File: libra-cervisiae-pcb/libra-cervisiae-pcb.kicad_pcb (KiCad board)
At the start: 2 copper layers, 63.8 x 43.2 mm, 24 parts, among them CN1 CP2102-BREAKOUT, CN2 HX711_BREAKOUT, J1 Wort Temp, J2 Ambient Temp, J3 Load Cells, SW1 Reset, SW2 Flash, U1 ESP32-WROOM-32, U2 VREG

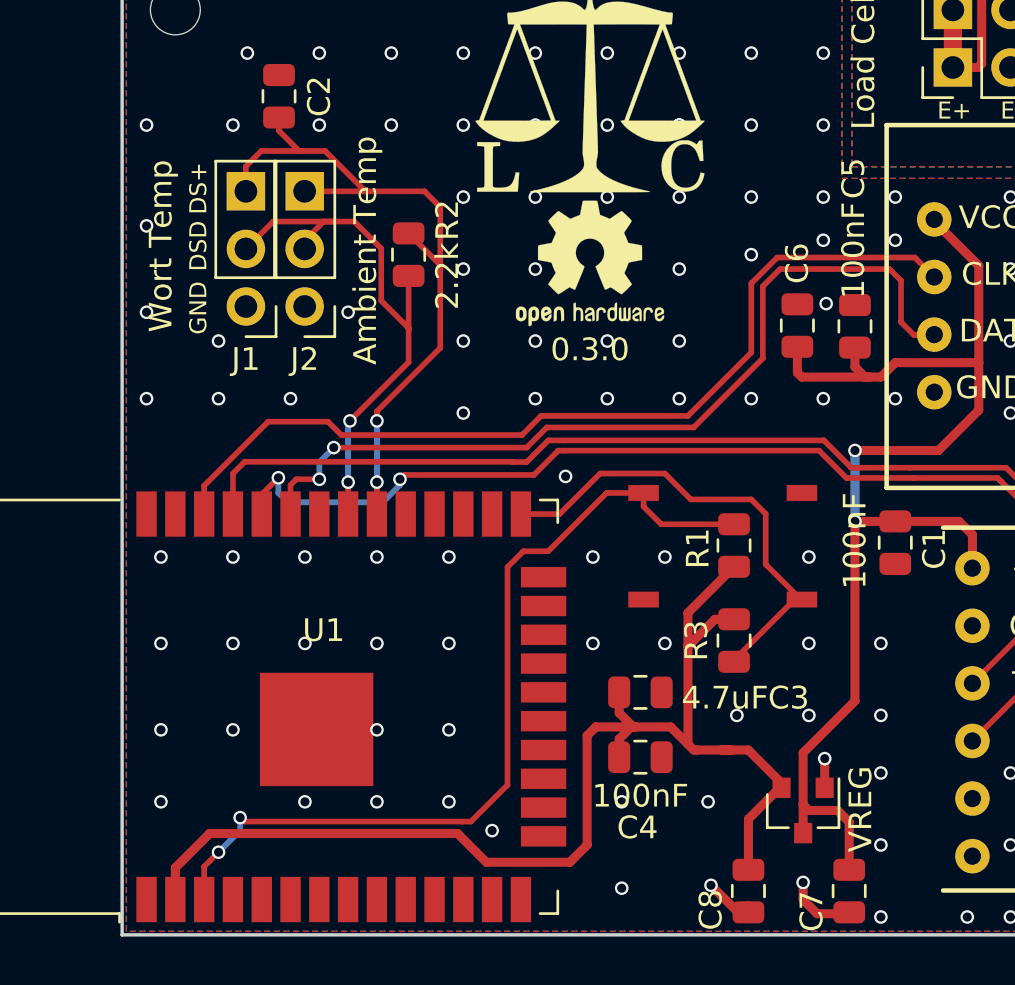
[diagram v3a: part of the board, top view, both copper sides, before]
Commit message: Add a Hotspot button to restart into hotspot mode
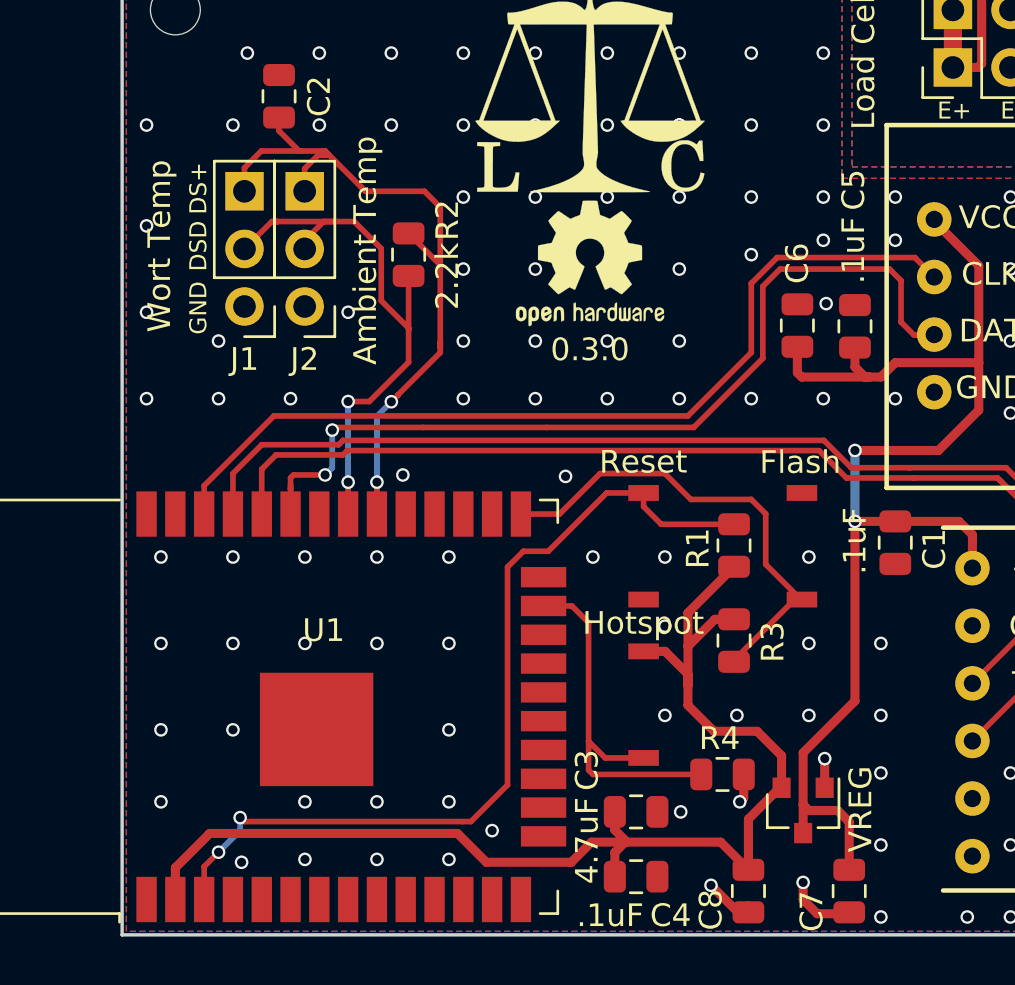
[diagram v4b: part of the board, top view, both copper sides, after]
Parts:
- added R4: 10k, Resistor_SMD:R_0805_2012Metric, F.Cu at (132.7, 101.7)
- added SW3: Hotspot, 4x3_SWITCH:4x3_Switch, F.Cu at (127.6, 95.9)
- C1, C4, C5: value 100nF -> .1uF
- moved C3 5.27 mm to (128.9, 103.3)
- moved C4 5.27 mm to (128.9, 106.2)
- moved J1 0.06 mm to (111.6, 81.0)
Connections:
- U1 pad 23: (no net) -> Net-(R4-Pad2)
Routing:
- net Net-(R4-Pad2): track 0.00 -> 16.4 mm
- net /GND: track 7.01 -> 8.29 mm, vias 164 -> 167
- net /DAT: track 38.1 -> 39.0 mm
- net /DSD: track 24.7 -> 25.5 mm
- net /HostTX: track 46.5 -> 46.6 mm, vias 2 -> 0

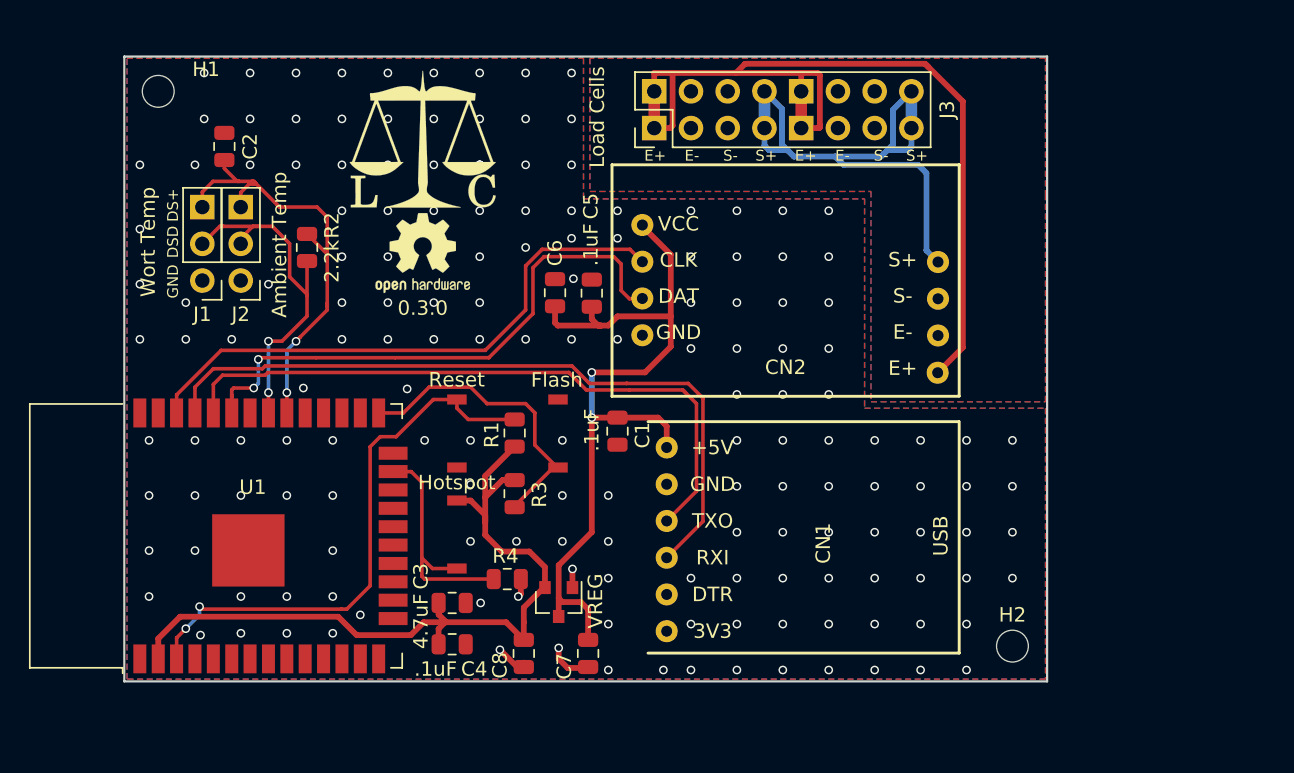
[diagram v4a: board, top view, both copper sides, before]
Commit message: Redo board to DP8049 size
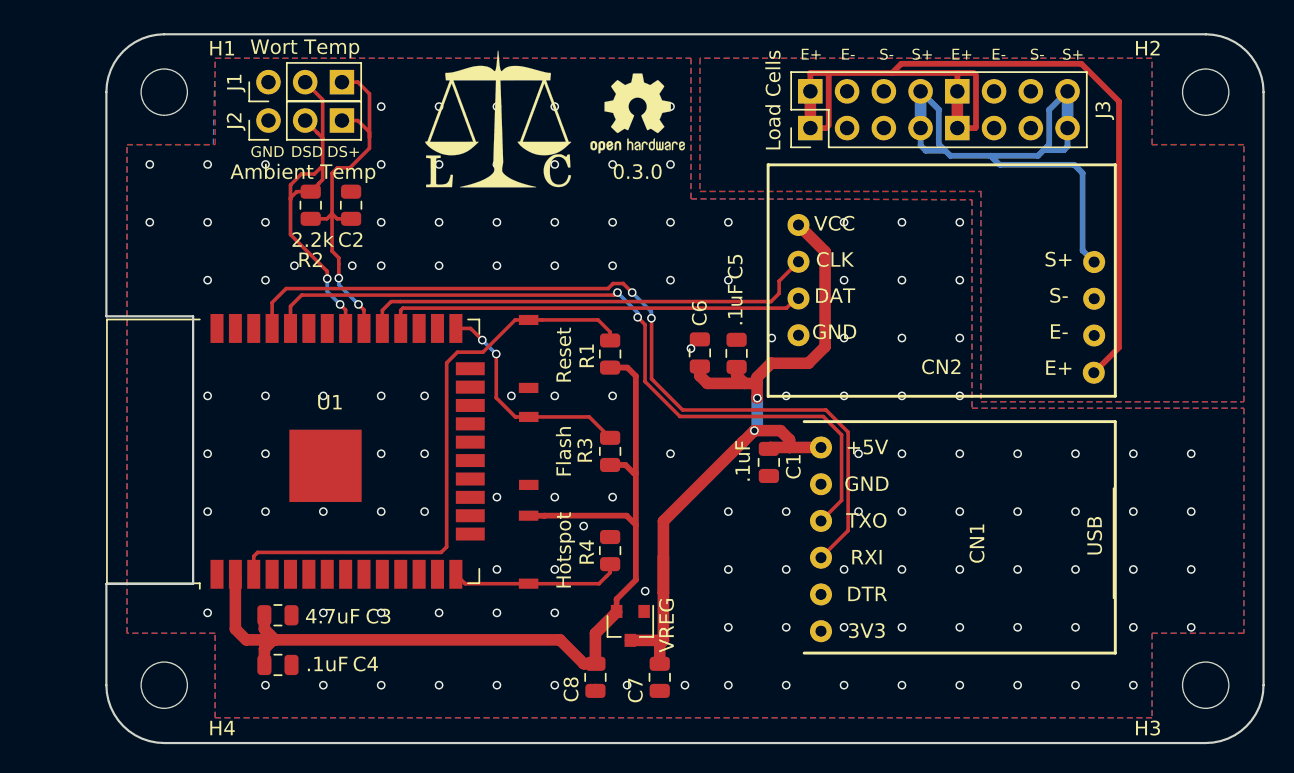
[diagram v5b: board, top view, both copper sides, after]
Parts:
- added H3: MountingHole_3.2mm_M3, MountingHole:MountingHole_3.2mm_M3, F.Cu at (181.0, 109.0)
- added H4: MountingHole_3.2mm_M3, MountingHole:MountingHole_3.2mm_M3, F.Cu at (109.0, 109.0)
- H1, H2: value MountingHole_2.2mm_M2 -> MountingHole_3.2mm_M3; footprint Mounting_Holes:MountingHole_2.2mm_M2 -> MountingHole:MountingHole_3.2mm_M3
- moved H2 40.6 mm to (181.0, 68.0)
- moved ? 17.7 mm to (141.7, 69.5)
- moved J1 14.5 mm to (116.2, 67.3), turned to 90 degrees
- moved C4 12.1 mm to (116.9, 107.6)
- moved C3 12.1 mm to (116.9, 104.2)
- moved J2 11.2 mm to (116.2, 70.0), turned to 90 degrees
- moved C5 10.8 mm to (148.6, 86.1)
- moved C6 10.8 mm to (146.0, 86.0)
- moved CN2 10.8 mm to (150.7, 73.0)
- moved J3 10.8 mm to (153.7, 70.5)
- moved C1 10.7 mm to (150.8, 93.6)
- moved CN1 10.7 mm to (174.6, 106.8)
- moved C2 9.66 mm to (121.9, 75.8)
- moved R1 8.57 mm to (139.8, 86.1)
- moved U1 7.91 mm to (120.9, 92.8)
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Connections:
- U1 pad 14: (no net) -> Net-(R4-Pad2)
- U1 pad 23: Net-(R4-Pad2) -> (no net)
- U1 pad 28: (no net) -> /DAT
- U1 pad 29: (no net) -> /CLK
- U1 pad 33: /DAT -> (no net)
- U1 pad 36: /CLK -> (no net)
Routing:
- net /3.3+: track 55.0 -> 70.6 mm
- net /DAT: track 39.0 -> 29.1 mm, vias 2 -> 0
- net /HostRX: track 50.5 -> 58.6 mm, vias 0 -> 2
- net /CLK: track 39.8 -> 31.9 mm
- net /GND: track 8.29 -> 0.90 mm, vias 167 -> 132
- net /HostTX: track 46.6 -> 53.1 mm, vias 0 -> 2
- net /DS+: track 32.6 -> 26.6 mm
- net Net-(R3-Pad1): track 20.9 -> 15.6 mm, vias 0 -> 2
- net Net-(R4-Pad2): track 16.4 -> 11.8 mm
- net /S+: track 44.2 -> 41.1 mm
- net Net-(R1-Pad1): track 38.7 -> 41.0 mm, vias 2 -> 0
- net /E+: track 66.9 -> 65.0 mm
- net /DSD: track 25.5 -> 26.1 mm
- net /USB+: track 55.8 -> 55.3 mm
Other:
- board size 63.8 x 43.2 mm -> 80 x 49 mm

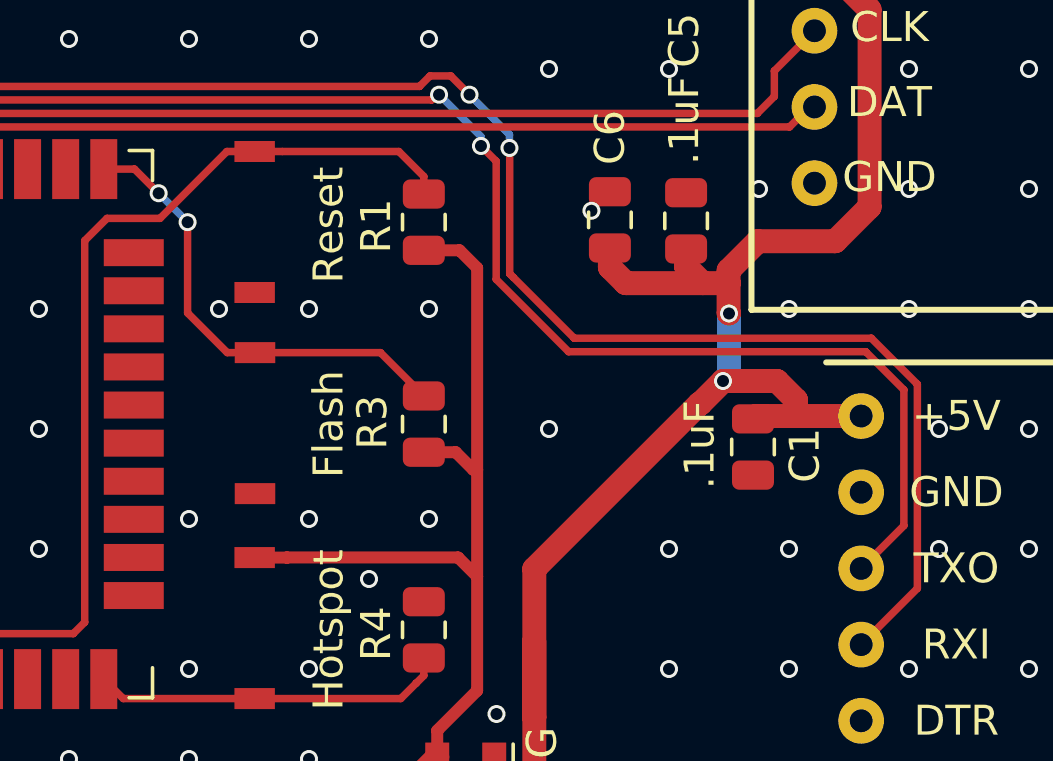
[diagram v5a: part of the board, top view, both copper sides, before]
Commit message: Ensure a via-free path from CP2012 to MCP1700
That seems like a recipe for making a super-hot via.
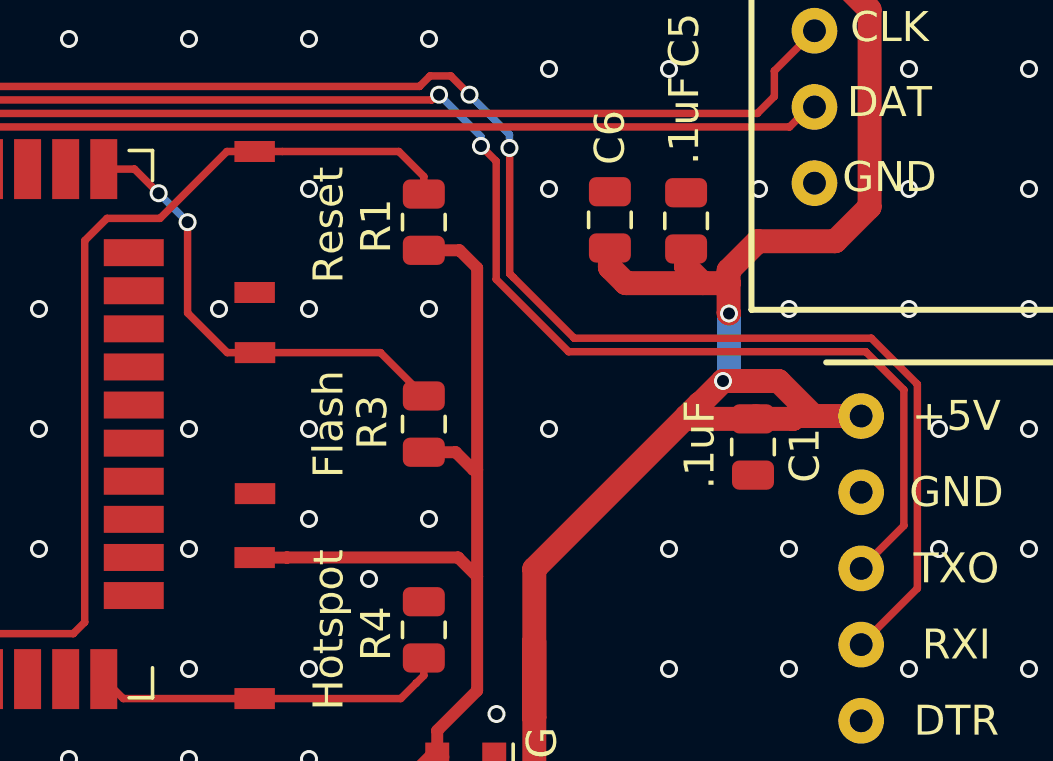
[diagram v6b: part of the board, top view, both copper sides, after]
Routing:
- net /USB+: track 55.3 -> 57.9 mm
- net /GND: vias 132 -> 135
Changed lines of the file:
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@@
     (thickness 1.6)
     (drawings 34)
-    (tracks 370)
+    (tracks 376)
     (zones 0)
     (modules 28)
@@
   )
   (setup
-    (last_trace_width 0.25)
+    (last_trace_width 0.8)
     (user_trace_width 0.4)
     (user_trace_width 0.8)
@@
   (segment (start 138.811 109.458) (end 138.414 109.458) (width 0.4) (layer F.Cu) (net 4) (status 30))
   (segment (start 138.811 109.331) (end 138.811 109.093) (width 0.4) (layer F.Cu) (net 4) (status 30))
-  (via (at 145.415 85.725) (size 0.6) (drill 0.4) (layers F.Cu B.Cu) (net 4))
   (via (at 142.25 102.5) (size 0.6) (drill 0.4) (layers F.Cu B.Cu) (net 4))
   (via (at 108 73) (size 0.6) (drill 0.4) (layers F.Cu B.Cu) (net 4))
@@
   (via (at 140 89) (size 0.6) (drill 0.4) (layers F.Cu B.Cu) (net 4))
   (via (at 140 96) (size 0.6) (drill 0.4) (layers F.Cu B.Cu) (net 4))
-  (via (at 136 96) (size 0.6) (drill 0.4) (layers F.Cu B.Cu) (net 4))
-  (via (at 132 96) (size 0.6) (drill 0.4) (layers F.Cu B.Cu) (net 4))
   (via (at 132 101) (size 0.6) (drill 0.4) (layers F.Cu B.Cu) (net 4))
   (via (at 136 101) (size 0.6) (drill 0.4) (layers F.Cu B.Cu) (net 4))
@@
   (via (at 116 109) (size 0.6) (drill 0.4) (layers F.Cu B.Cu) (net 4))
   (via (at 112 104) (size 0.6) (drill 0.4) (layers F.Cu B.Cu) (net 4))
+  (via (at 144 85) (size 0.6) (drill 0.4) (layers F.Cu B.Cu) (net 4))
+  (via (at 136 85) (size 0.6) (drill 0.4) (layers F.Cu B.Cu) (net 4))
+  (via (at 132 93) (size 0.6) (drill 0.4) (layers F.Cu B.Cu) (net 4))
+  (via (at 136 93) (size 0.6) (drill 0.4) (layers F.Cu B.Cu) (net 4))
+  (via (at 132 97) (size 0.6) (drill 0.4) (layers F.Cu B.Cu) (net 4))
+  (via (at 136 96) (size 0.6) (drill 0.4) (layers F.Cu B.Cu) (net 4))
   (segment (start 150.8955 92.567) (end 150.8 92.6625) (width 0.8) (layer F.Cu) (net 5) (status 30))
-  (segment (start 152.233 92.567) (end 152.233 92.033) (width 0.8) (layer F.Cu) (net 5))
-  (segment (start 152.233 92.567) (end 150.8955 92.567) (width 0.8) (layer F.Cu) (net 5) (status 20))
-  (segment (start 154.405 92.567) (end 152.233 92.567) (width 0.8) (layer F.Cu) (net 5) (status 10))
-  (segment (start 152.233 92.033) (end 151.6 91.4) (width 0.8) (layer F.Cu) (net 5))
-  (segment (start 151.6 91.4) (end 149.8 91.4) (width 0.8) (layer F.Cu) (net 5))
   (segment (start 149.8 91.4) (end 149.0465 92.1535) (width 0.8) (layer F.Cu) (net 5))
   (segment (start 143.256 106.164) (end 143.256 107.5205) (width 0.8) (layer F.Cu) (net 5) (status 20))
@@
   (segment (start 143.51 97.663) (end 143.51 102.616) (width 0.8) (layer F.Cu) (net 5))
   (segment (start 143.51 100.076) (end 143.51 102.616) (width 0.8) (layer F.Cu) (net 5))
-  (segment (start 149.0195 92.1535) (end 143.51 97.663) (width 0.8) (layer F.Cu) (net 5))
   (segment (start 143.51 102.616) (end 143.51 105.91) (width 0.8) (layer F.Cu) (net 5))
   (via (at 150 89.15) (size 0.6) (drill 0.4) (layers F.Cu B.Cu) (net 5))
@@
   (segment (start 150 89.15) (end 150 91.2) (width 0.8) (layer B.Cu) (net 5))
   (segment (start 150 91.2) (end 149.8 91.4) (width 0.8) (layer B.Cu) (net 5))
+  (segment (start 152.1375 92.6625) (end 148.6625 92.6625) (width 0.8) (layer F.Cu) (net 5))
+  (segment (start 148.6625 92.6625) (end 148.5865 92.5865) (width 0.8) (layer F.Cu) (net 5))
+  (segment (start 152.233 92.567) (end 152.1375 92.6625) (width 0.8) (layer F.Cu) (net 5))
+  (segment (start 149.0195 92.1535) (end 148.5865 92.5865) (width 0.8) (layer F.Cu) (net 5))
+  (segment (start 148.5865 92.5865) (end 143.51 97.663) (width 0.8) (layer F.Cu) (net 5))
+  (segment (start 151.65 91.4) (end 152.817 92.567) (width 0.8) (layer F.Cu) (net 5))
+  (segment (start 149.8 91.4) (end 151.65 91.4) (width 0.8) (layer F.Cu) (net 5))
+  (segment (start 154.405 92.567) (end 152.817 92.567) (width 0.8) (layer F.Cu) (net 5))
+  (segment (start 152.817 92.567) (end 152.233 92.567) (width 0.8) (layer F.Cu) (net 5))
   (segment (start 152.685 82.265) (end 152.849 82.265) (width 0.25) (layer F.Cu) (net 6))
   (segment (start 125.505 82.931) (end 152.019 82.931) (width 0.25) (layer F.Cu) (net 6))

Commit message: Minor PCB updates for ordering
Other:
- outline, holes or cut-outs redrawn
- rule solder_mask_min_width: 0.25 -> 0.15
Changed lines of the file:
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@@
   )
   (setup
-    (last_trace_width 0.8)
+    (last_trace_width 0.25)
     (user_trace_width 0.4)
     (user_trace_width 0.8)
@@
     (mod_text_size 1 1)
     (mod_text_width 0.15)
-    (pad_size 5 5)
+    (pad_size 2 0.9)
     (pad_drill 0)
     (pad_to_mask_clearance 0.2)
-    (solder_mask_min_width 0.25)
+    (solder_mask_min_width 0.15)
     (aux_axis_origin 11.938 11.938)
     (visible_elements FFFFFFFF)
@@
     (descr "Single 2.4 GHz Wi-Fi and Bluetooth combo chip https://www.espressif.com/sites/default/files/documentation/esp32-wroom-32_datasheet_en.pdf")
     (tags "Single 2.4 GHz Wi-Fi and Bluetooth combo  chip")
+    (solder_mask_margin 0.1)
+    (solder_paste_ratio -0.1)
     (attr smd)
-    (fp_text reference U1 (at 3.3655 -0.4445) (layer F.SilkS)
-      (effects (font (size 1 1) (thickness 0.15)))
-    )
-    (fp_text value ESP32-WROOM-32 (at 5.588 0.254 180) (layer F.Fab)
+    (fp_text reference U1 (at 3.3655 -0.4445 180) (layer F.SilkS)
+      (effects (font (size 1 1) (thickness 0.15)))
+    )
+    (fp_text value ESP32-WROOM-32 (at 5.588 0.254) (layer F.Fab)
       (effects (font (size 1 1) (thickness 0.15)))
     )
     (fp_line (start -9.12 -9.445) (end -9.5 -9.445) (layer F.SilkS) (width 0.12))
-    (fp_line (start -9.12 -15.865) (end -9.12 -9.445) (layer F.SilkS) (width 0.12))
-    (fp_line (start 9.12 -15.865) (end 9.12 -9.445) (layer F.SilkS) (width 0.12))
-    (fp_line (start -9.12 -15.865) (end 9.12 -15.865) (layer F.SilkS) (width 0.12))
+    (fp_line (start -9.12 -15.865) (end -9.12 -9.445) (layer Dwgs.User) (width 0.12))
+    (fp_line (start 9.12 -15.865) (end 9.12 -9.445) (layer Dwgs.User) (width 0.12))
+    (fp_line (start -9.12 -15.865) (end 9.12 -15.865) (layer Dwgs.User) (width 0.12))
     (fp_line (start 9.12 9.88) (end 8.12 9.88) (layer F.SilkS) (width 0.12))
     (fp_line (start 9.12 9.1) (end 9.12 9.88) (layer F.SilkS) (width 0.12))
@@
     (fp_line (start 9 9.76) (end 9 -15.745) (layer F.Fab) (width 0.1))
     (fp_line (start -14 -9.97) (end -14 -20.75) (layer Dwgs.User) (width 0.1))
-    (fp_text user "5 mm" (at 7.8 -19.075) (layer Cmts.User)
+    (fp_text user "5 mm" (at 7.8 -19.075 180) (layer Cmts.User)
       (effects (font (size 0.5 0.5) (thickness 0.1)))
     )
@@
     (arrow2b (pts (xy 105 57.75) (xy 106.126504 57.163579)))
   )
-  (gr_line (start 111 102) (end 105 102) (layer Edge.Cuts) (width 0.15))
-  (gr_line (start 111 83.5) (end 111 102) (layer Edge.Cuts) (width 0.15))
+  (gr_line (start 111 102.2) (end 105 102.2) (layer Edge.Cuts) (width 0.15))
+  (gr_line (start 111 83.5) (end 111 102.2) (layer Edge.Cuts) (width 0.15))
   (gr_line (start 105 83.5) (end 111 83.5) (layer Edge.Cuts) (width 0.15))
   (gr_line (start 105 83.5) (end 105 68) (angle 90) (layer Edge.Cuts) (width 0.15))
@@
   (gr_line (start 185 68) (end 185 109) (angle 90) (layer Edge.Cuts) (width 0.15))
   (gr_line (start 109 64) (end 181 64) (angle 90) (layer Edge.Cuts) (width 0.15))
-  (gr_line (start 105 109) (end 105 102) (angle 90) (layer Edge.Cuts) (width 0.15))
+  (gr_line (start 105 109) (end 105 102.2) (angle 90) (layer Edge.Cuts) (width 0.15))
   (gr_text 0.3.0 (at 141.732 73.533) (layer F.SilkS)
     (effects (font (size 1 1) (thickness 0.15)))
@@
     (polygon
       (pts
-        (xy 111 107.25) (xy 99.75 107.25) (xy 99.75 78.5) (xy 111 78.5)
+        (xy 111 107.25) (xy 99.75 107.25) (xy 99.75 78.4) (xy 111 78.4)
       )
     )
